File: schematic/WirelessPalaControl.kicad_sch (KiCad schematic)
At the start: 20 parts, among them J1 6P6C, J2 MCU UART, Q1 BC847B, Q2 BC847B, U1 SI8621, U2 WeMos_mini

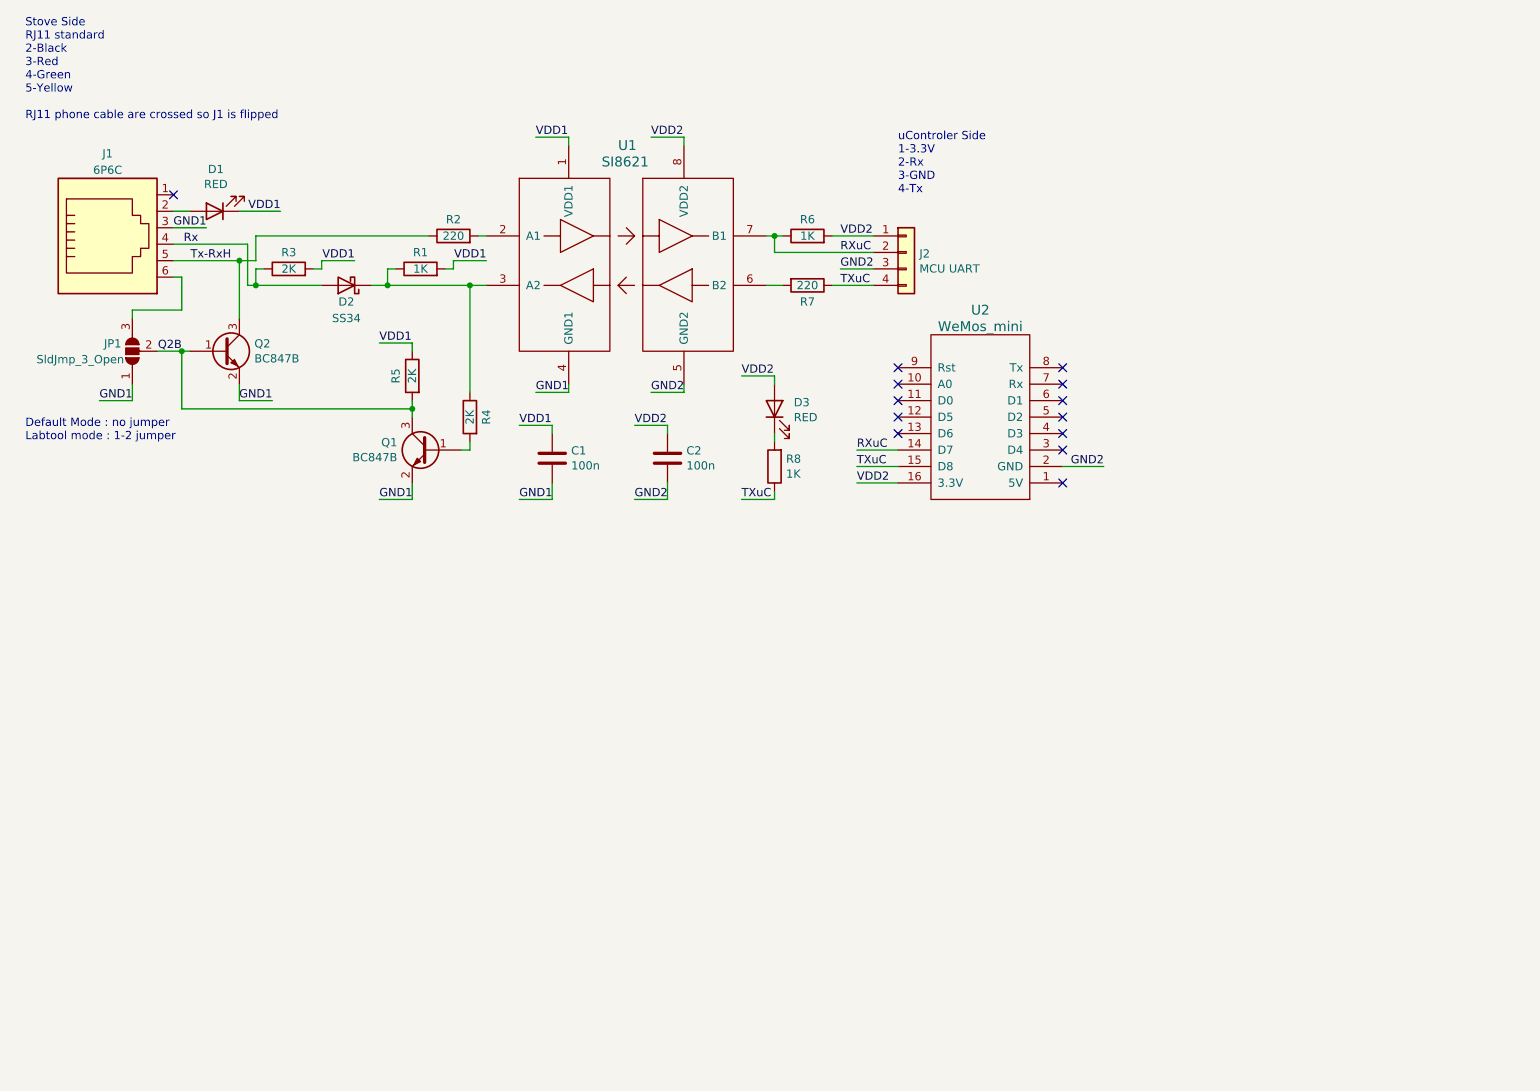
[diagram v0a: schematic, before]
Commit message: New Hardware Version (V2.0) (#65)
* Add hw version detection

* New PCB version

* Implement Hardware detection

* Do Not Place J2

* New box

* Update box

* Update box img

* Update schematic

* Update pcb img

* Update cabling img

* Update BUILD.md

* Update cabling part in README.md

* Change R4 to 2K

* Update schematic and botoom pcb

* Slightly adjust box
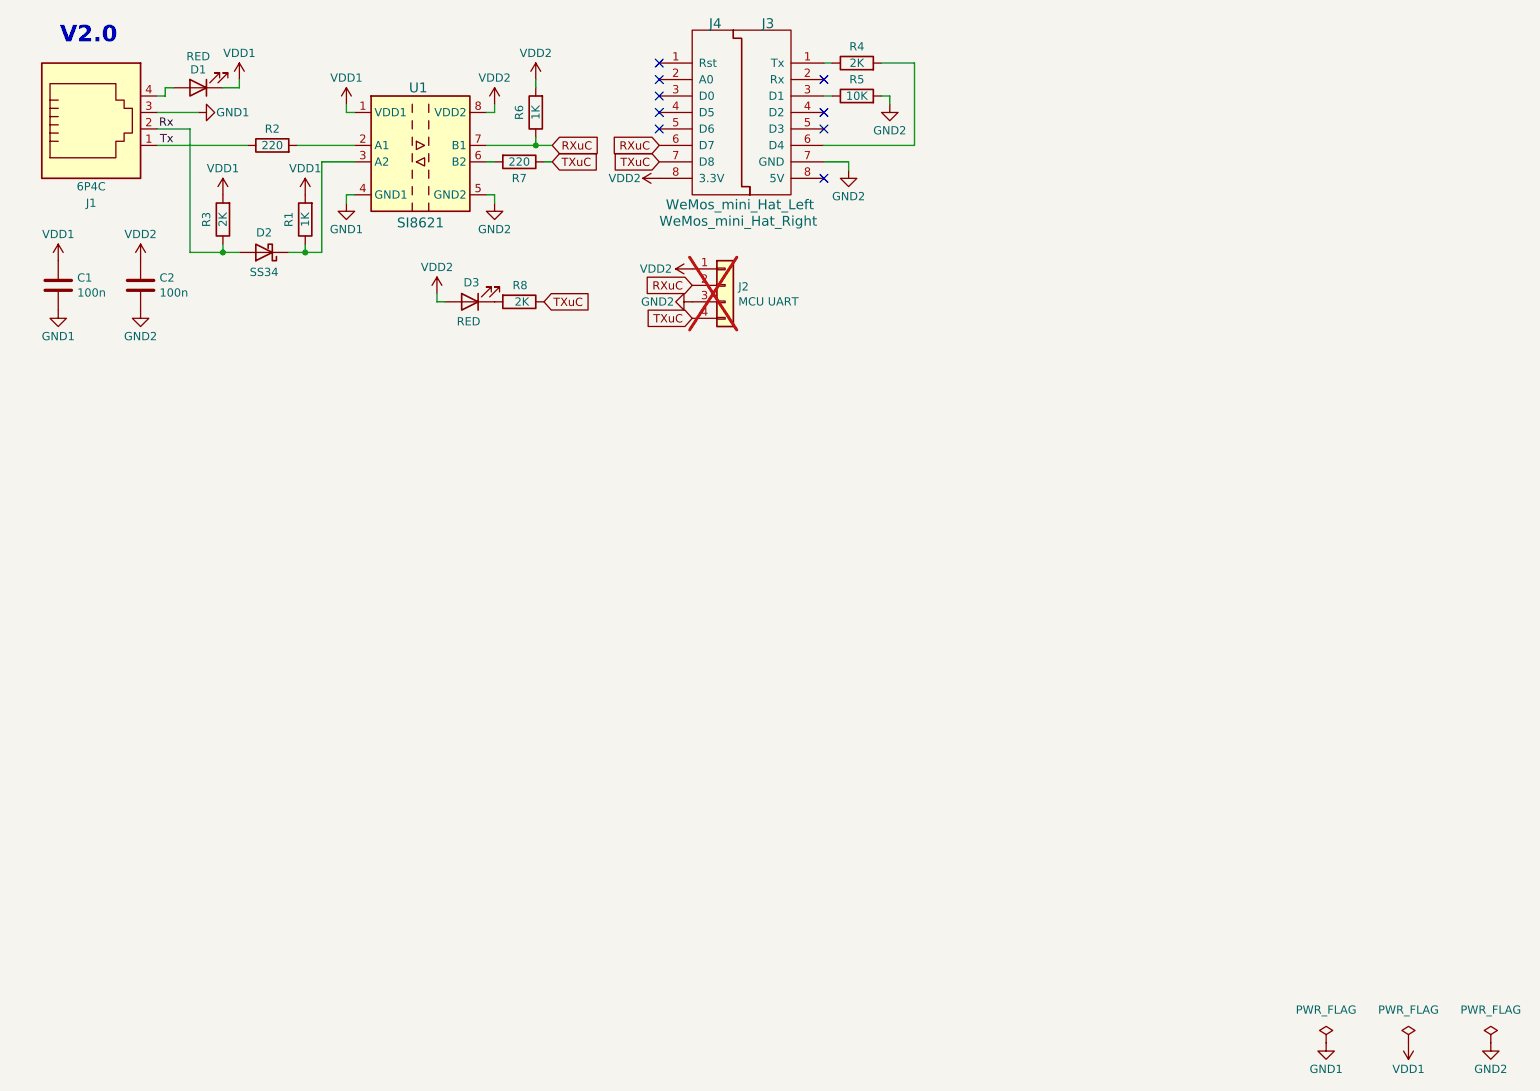
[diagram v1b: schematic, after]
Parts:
- removed JP1: SldJmp_3_Open, Jumper:SolderJumper-3_P1.3mm_Open_Pad1.0x1.5mm_NumberLabels, symbol Jumper:SolderJumper_3_Open
- removed Q1, Q2: BC847B, Package_TO_SOT_SMD:SOT-23_Handsoldering, symbol Transistor_BJT:BC847
- removed U2: WeMos_mini, wemos_d1_mini:wemos-d1-mini-DIL-only, symbol wemos_mini:WeMos_mini
- added J3: WeMos_mini_Hat_Left, wemos_d1_mini:WeMos_D1_mini_Hat_Left, symbol wemos_mini:WeMos_D1_mini_Hat_Left
- added J4: WeMos_mini_Hat_Right, wemos_d1_mini:WeMos_D1_mini_Hat_Right, symbol wemos_mini:WeMos_D1_mini_Hat_Right
- C1, C2: footprint Capacitor_SMD:C_0805_2012Metric_Pad1.15x1.40mm_HandSolder -> Capacitor_SMD:C_0805_2012Metric_Pad1.18x1.45mm_HandSolder; LCSC (none) -> C49678
- D1, D3: LCSC (none) -> C84256
- D2: LCSC (none) -> C8678
- J1: value 6P6C -> 6P4C; footprint MyRJ:Ali_RJ12 -> MyRJ:Ali_RJ11; symbol Connector:6P6C -> Connector:6P4C; JlcPosOffset (none) -> 0,3.07; JlcRotOffset (none) -> 180; LCSC (none) -> C189749
- J2: now not fitted; now left out of the parts list
- R1, R6: footprint Resistor_SMD:R_0805_2012Metric_Pad1.15x1.40mm_HandSolder -> Resistor_SMD:R_0805_2012Metric_Pad1.20x1.40mm_HandSolder; LCSC (none) -> C17513
- R2, R7: footprint Resistor_SMD:R_0805_2012Metric_Pad1.15x1.40mm_HandSolder -> Resistor_SMD:R_0805_2012Metric_Pad1.20x1.40mm_HandSolder; LCSC (none) -> C17557
- R3, R4: footprint Resistor_SMD:R_0805_2012Metric_Pad1.15x1.40mm_HandSolder -> Resistor_SMD:R_0805_2012Metric_Pad1.20x1.40mm_HandSolder; LCSC (none) -> C17604
- R5: value 2K -> 10K; footprint Resistor_SMD:R_0805_2012Metric_Pad1.15x1.40mm_HandSolder -> Resistor_SMD:R_0805_2012Metric_Pad1.20x1.40mm_HandSolder; LCSC (none) -> C17414
- R8: value 1K -> 2K; footprint Resistor_SMD:R_0805_2012Metric_Pad1.15x1.40mm_HandSolder -> Resistor_SMD:R_0805_2012Metric_Pad1.20x1.40mm_HandSolder; LCSC (none) -> C17604
- U1: symbol si8621:SI8621 -> si8621:Si8621EC-B-IS; LCSC (none) -> C461877
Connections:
- net Q2B is gone; now on net GND2: R5.2
- net GND2: now also J3.7 (GND)
- net RXuC: now also J4.6 (D7)
- net Rx: now also J1.2; no longer J1.4
- net TXuC: now also J4.7 (D8)
- net VDD1: no longer R5.1
- net VDD2: now also J4.8 (3.3V)
- net at D2.1 (K), R1.1, U1.3 (A2): no longer R4.1
- net at R4.2: now also J3.6 (D4)
- net Tx: now reaches J1.1
- net Tx: now also R2.1
- net at D1.2 (A): now also J1.4; no longer J1.2
- removed net Tx-RxH: J1.5, R2.1
- new net: J3.3 (D1), R5.1
- new net: J3.1 (Tx), R4.1
- no-connect marks 13 -> 9
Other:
- note added: "V2.0"
- note removed: "Default Mode : no jumper Labtool mode : 1-2 jumper"
- note removed: "Stove Side RJ11 standard 2-Black 3-Red 4-Green 5-Yellow RJ11 phone cable are crossed so J1 is flipped"
- note removed: "uControler Side 1-3.3V 2-Rx 3-GND 4-Tx"
- moved on the sheet: C1, C2, D1, D2, D3, R1, R2, R3, R6, R7, R8, U1
